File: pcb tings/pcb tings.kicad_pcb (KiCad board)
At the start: 2 copper layers, 77 x 38.1 mm, 24 parts, among them SW1 SW_Push, U1 ATmega32U4-A, Y1 16MHz

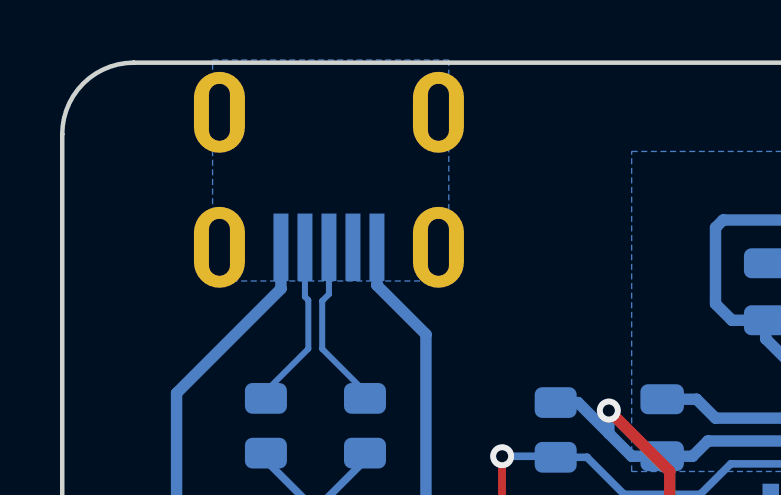
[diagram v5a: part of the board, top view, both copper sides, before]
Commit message: fixed USB connection error DRC
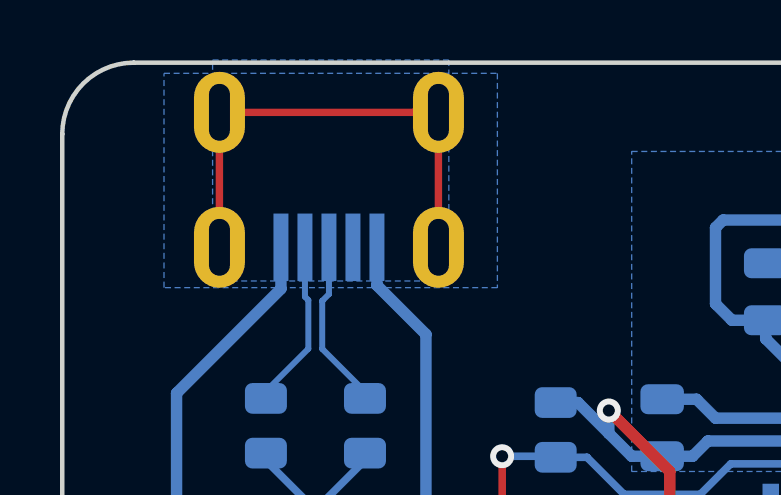
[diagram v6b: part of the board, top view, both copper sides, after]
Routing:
- net unconnected-(USB1-Pad6): track 0.00 -> 16.3 mm
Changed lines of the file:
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@@
   (segment (start 102.195936 91.781936) (end 103.124 92.71) (width 0.254) (layer "B.Cu") (net 26))
   (segment (start 84.328 83.312) (end 87.122 86.106) (width 0.254) (layer "B.Cu") (net 26))
+  (segment (start 50.26684 63.211436) (end 57.56684 63.211436) (width 0.25) (layer "F.Cu") (net 37))
+  (segment (start 50.26684 63.211436) (end 50.26684 67.711436) (width 0.25) (layer "F.Cu") (net 37))
+  (segment (start 57.56684 63.211436) (end 57.56684 67.711436) (width 0.25) (layer "F.Cu") (net 37))
   (segment (start 55.118 72.523782) (end 55.118 72.7475) (width 0.2) (layer "B.Cu") (net 38))
   (segment (start 53.692369 69.497631) (end 53.692369 71.098151) (width 0.2) (layer "B.Cu") (net 38))
@@
       )
     )
+  )
+  (zone (net 2) (net_name "GND") (layer "B.Cu") (hatch edge 0.508)
+    (connect_pads (clearance 0.508))
+    (min_thickness 0.254) (filled_areas_thickness no)
+    (fill yes (thermal_gap 0.508) (thermal_bridge_width 0.508))
+    (polygon
+      (pts
+        (xy 59.53125 69.05625)
+        (xy 48.41875 69.05625)
+        (xy 48.41875 61.9125)
+        (xy 59.53125 61.9125)
+      )
+    )
